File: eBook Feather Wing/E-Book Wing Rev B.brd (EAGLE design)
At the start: 77.5 x 107.4 mm, 92 parts, among them IC1 MCP23008/SO, IC2 23K256-I/SN, J1 MJ-3502N, Q1 IRLML0100, Q2 BSS138, Q3 DMG3415, SW1 SPDT_SWITCH

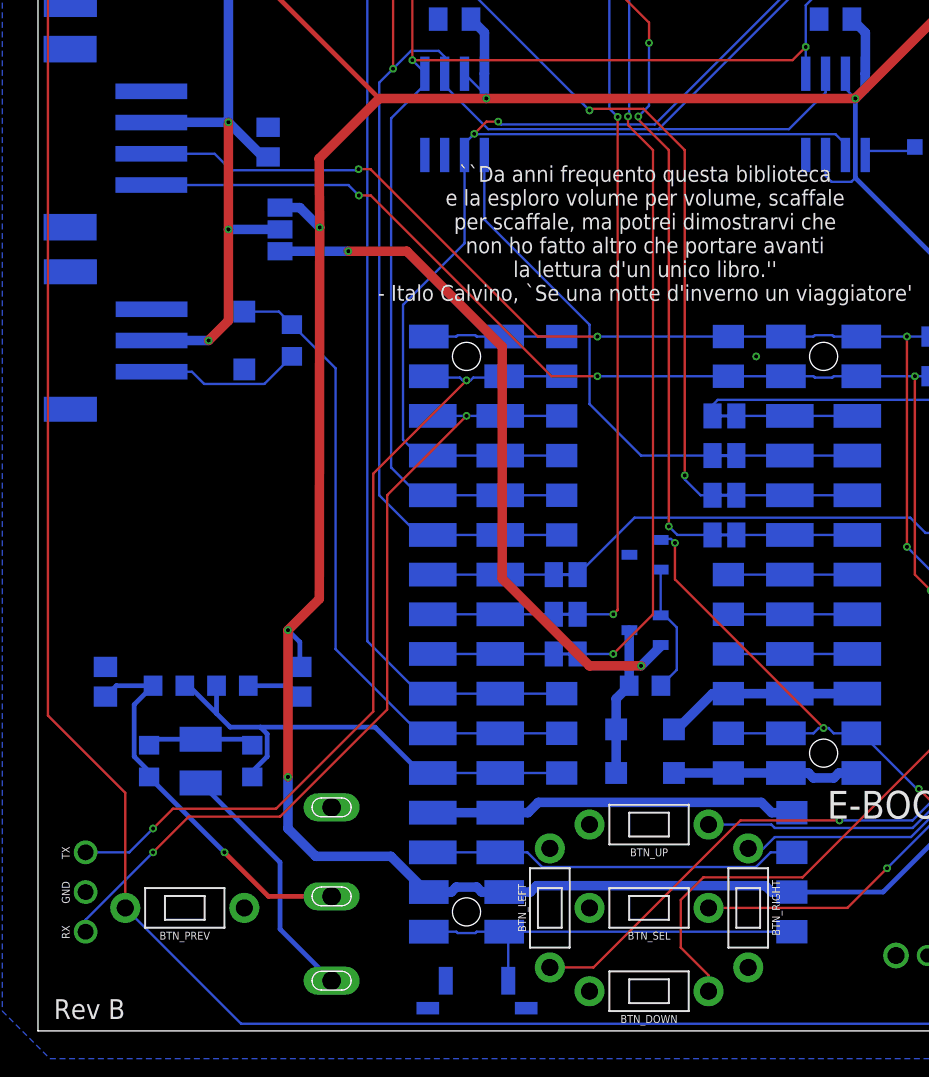
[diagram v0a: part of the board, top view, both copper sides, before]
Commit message: remove 5V option, more complicated than I thought
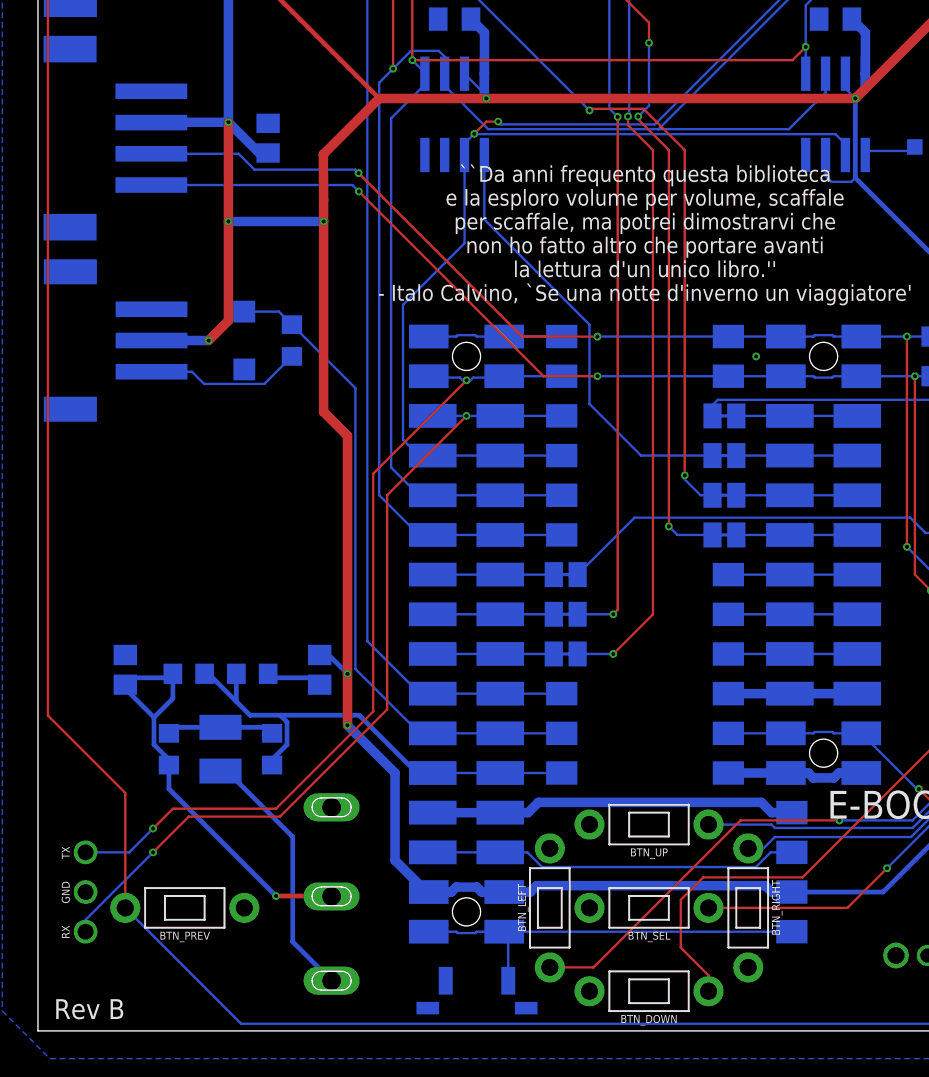
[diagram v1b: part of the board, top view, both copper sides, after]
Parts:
- removed D6, D7: MBR120, microbuilder:SOD-123
- removed Q2: BSS138, pygamer-microbuilder:SOT23-R
- removed Q3: DMG3415, pygamer-microbuilder:SOT23-R
- removed R10: 100K, microbuilder:_0805MP
- removed SJ1: (no value), pygamer-microbuilder:SOLDERJUMPER_2WAY_OPEN_NOPASTE
- moved R9 1.48 mm to (8.13, 18.0)
- moved C6 1.48 mm to (11.4, 18.0)
- moved FB1 1.48 mm to (17.8, 23.1)
- moved FB2 1.48 mm to (5.33, 23.1)
- moved R6 1.48 mm to (13.5, 22.9)
- moved R7 1.48 mm to (9.40, 22.9)
- moved R8 1.48 mm to (14.7, 18.0)
- moved C1 0.25 mm to (14.5, 57.1)
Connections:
- removed net !EN: Q2.1, Q3.2, R10.1
- removed net +5V: Q2.2, SJ1.1
- removed net N$7: D6.C, D7.C, Q2.3, R10.2
- removed net V+: A1_PORT.2, A2_PORT.2, C1.1, I2C.2, SJ1.2
- net +3V3: now also A1_PORT.2, A2_PORT.2, C1.1, I2C.2; no longer SJ1.3
- net EN: no longer Q3.1
- net GND: no longer Q3.3
- net VBAT: no longer D7.A
- net VBUS: no longer D6.A
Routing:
- net V+: track 45.5 -> 0.00 mm, vias 3 -> 0
- net +5V: track 44.7 -> 0.00 mm, vias 2 -> 0
- net +3V3: track 298.3 -> 338.3 mm, vias 9 -> 12
- net EN: track 42.5 -> 25.5 mm, vias 3 -> 1
- net N$7: track 9.50 -> 0.00 mm
- net !EN: track 8.43 -> 0.00 mm
- net VBUS: track 12.7 -> 8.26 mm
- net VBAT: track 12.3 -> 8.77 mm
- net AGND: track 24.9 -> 27.7 mm
- net A0: track 32.0 -> 31.0 mm
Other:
- board text added: "ENABLE_SWITCH"
- board text added: "HEADPHONE JACK"
- board text added: "The DAC on A0 drives mono jack J1. Ferrite beads FB1 & FB2 isolate this analog circuit to reduce noise. R6 & R7 act as a voltage divider on 3V to set the bias of the output signal. Then C6, a large coupling capacitor, lets audible frequencies pass while blocking any DC bias."
- board text removed: "+VOLTAGE SELECT!"
- board text removed: "5V"
- board text removed: "5V to ports v"
- board text removed: "Easy way: Close SJ1 to 3V and you're done. If you want to power 5V devices, close SJ1 to 5V and populate: D6 & D7 (to get the higher of VBAT & VBUS), Q3 (to invert EN), Q2 (to switch 5V on when Feather is enabled) and R10 (pullup for !EN!)."
- board text removed: "HEADPHONE JACK (A0)"
- board text removed: "Only needed for 5V on <-JST ports! See voltage select note at right."
- board text removed: "higher power"

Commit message: final commit of rev B as submitted to OSH Park
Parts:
- added BTN_LOCK: SPST_TACTILE_SWITCHRA, My Stuff:TL3330AF130QG
- added FID1, FID2, FID3, FID4: FIDUCIAL_1MM, microbuilder:FIDUCIAL_1MM
- added JP2: (no value), adafruit:1X01
- added U$1, U$4, U$5, U$7: MOUNTINGHOLE2.5, microbuilder:MOUNTINGHOLE_2.5_PLATED
- moved JP1 100.2 mm to (8.64, 109.0), turned to 0 degrees
- moved FB1 4.89 mm to (15.5, 18.8)
- moved FB2 4.89 mm to (3.05, 18.8)
- moved C6 4.89 mm to (9.14, 13.7)
- moved R8 4.89 mm to (12.4, 13.7)
- moved R9 4.89 mm to (5.84, 13.7)
- moved R6 4.89 mm to (11.2, 18.5)
- moved R7 4.89 mm to (7.11, 18.5)
- moved GOLD_ORB_SM1 4.42 mm to (68.1, 4.06)
- moved MICROSD 0.38 mm to (61.1, 82.0)
- moved BTN_NEXT_ALT 0.15 mm to (74.3, 90.9)
- moved BTN_PREV_ALT 0.15 mm to (2.64, 91.4)
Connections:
- new net BTN_LOCK: BTN_LOCK.P$1, IC1.17
- net +3V3: now also JP2.1
- net GND: now also BTN_LOCK.P$2
- net SD_CD: no longer IC1.17
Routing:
- net BTN_LOCK: track 0.00 -> 91.0 mm, vias 0 -> 2
- net SD_CD: track 57.4 -> 0.00 mm, vias 2 -> 0
- net RX: track 54.8 -> 86.9 mm, vias 2 -> 3
- net +3V3: track 338.3 -> 367.2 mm, vias 12 -> 11
- net TX: track 54.5 -> 83.0 mm, vias 2 -> 3
- net GND: track 23.5 -> 0.00 mm, vias 5 -> 8
- net A0: track 31.0 -> 37.7 mm, vias 0 -> 2
- net AUDIO_OUT: track 16.6 -> 13.9 mm
- net AGND: track 27.7 -> 30.1 mm
- net BTN_LEFT: track 54.6 -> 55.4 mm
- net PREVGL: track 44.4 -> 43.8 mm
- net BTN_NEXT: track 88.7 -> 89.2 mm
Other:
- board size 77.5 x 107.4 mm -> 77.5 x 111.3 mm
- board text added: ">1 NC 2 N-Channel MOSFET Gate Drive Control 3 Current Sense Input for Control Loop 4 Negative Gate driving voltage 5 Positive Gate driving voltage 6 Clock for external LM75 temp sensor 7 Data for external LM75 temp sensor 8 Bus selection pin (tied to GND) 9 Busy state output pin (EBSY) 10 Reset (ERST) 11 Data / Command input pin (EDC) 12 Chip Select input pin (ECS) 13 Serial clock pin (SPI: SCK) 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"
- board text added: "A microSD card interfaces with the Feather mainboard via the SPI interface (MISO, MOSI, SCK, SDCS). C2 is a filtering cap for the SD card's power supply."
- board text added: "BTN_LOCK"
- board text added: "Bits: 0: LEFT 1: DOWN 2: UP 3: RIGHT 4: SEL 5: PREV 6: NEXT 7: LOCK"
- board text added: "Project info:"
- board text added: "The 23K256-I/SN SRAM chip provides a buffer for the display. It uses the SPI interface + SRCS. A B&W 400x300 display requires 15000 bytes; if you have that RAM to spare, omit this chip (and C4)."
- board text added: "The DAC on A0 drives mono headphone jack J1. FB1 & FB2 are ferrite beads that isolate this analog circuit from the rest of the board. R6 & R7 act as a voltage divider on the isolated 3V to set the bias of the output signal. C6 acts as a coupling capacitor; it lets the AC component of the output signal pass to the headphone jack, while blocking the DC component."
- board text added: "The MCP23008 provides eight additional GPIO pins via the I2C interface. It connects to all buttons except for RESET. R3 and R4 are the pull-up resistors for, respectively, SDA and SCL. This chip is required to use the buttons, unless you just want a few wired directly to GPIO pads. Capacitor C3 filters power."
- board text added: "These are the Feather's UART pins, plus a 3V pin if you need to power something like a GPS. Toss some right angle header on here, it might prove useful."
- board text added: "This bit is unrelated, just an extra spot for <- a `Next Page' button."
- board text added: "github.com/joeycastillo/The-Open-Book"
- board text removed: ">1 NC 2 N-Channel MOSFET Gate Drive Control 3 Current Sense Input for Control Loop 4 Negative Gate driving voltage 5 Positive Gate driving voltage 6 Clock for external LM75 temp sensor 7 Data for external LM75 temp sensor 8 Bus selection pin (tied to GND) 9 Busy state output pin 10 Reset 11 Data / Command control pin 12 Chip Select input pin 13 Serial clock pin (SPI) 14 Serial data pin (SPI) 15 P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"
- board text removed: "A microSD card interfaces with the Feather mainboard via the SPI interface (MISO, MOSI, SCK, SDCS). The card detect line is available via the GPIO expander's high bit. C2 is a filtering cap for the SD card's power supply."
- board text removed: "Bits: 0: LEFT 1: DOWN 2: UP 3: RIGHT 4: SEL 5: PREV 6: NEXT 7: SD CD"
- board text removed: "CARD DET"
- board text removed: "I brought the Feather's UART pins out here. Might as well toss some right angle header on JP1, might turn out to be useful."
- board text removed: "The 23K256-I/SN SRAM chip provides a buffer for the display. It uses the SPI interface + SRCS. A B&W 400x300 display requires 16000 bytes; if you have that RAM to spare, omit this chip (and C4)."
- board text removed: "The DAC on A0 drives mono jack J1. Ferrite beads FB1 & FB2 isolate this analog circuit to reduce noise. R6 & R7 act as a voltage divider on 3V to set the bias of the output signal. Then C6, a large coupling capacitor, lets audible frequencies pass while blocking any DC bias."
- board text removed: "The MCP23008 provides eight additional GPIO pins via the I2C interface. It connects to all buttons (except for RESET) as well as the SD slot's card detect signal. R3 and R4 are the pull-up resistors for SDA and SCL, respectively. This chip is required to use the buttons unless you just want a few wired directly to GPIO pads. Capacitor C3 filters power."
- board text removed: "This bit is unrelated, just <- an extra spot for a `Next Page' button."

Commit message: final tweaks and BOM for rev B
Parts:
- L1: value 68uH -> 10uH
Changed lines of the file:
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@@
 <attribute name="VALUE" x="44.45" y="78.486" size="0.508" layer="28" font="vector" ratio="18" rot="MR270" align="center"/>
 </element>
-<element name="L1" library="microbuilder" package="INDUCTOR_4X4MM_NR401" value="68uH" x="38.1" y="77.216" smashed="yes" rot="MR90">
+<element name="L1" library="microbuilder" package="INDUCTOR_4X4MM_NR401" value="10uH" x="38.1" y="77.216" smashed="yes" rot="MR90">
 <attribute name="NAME" x="38.1" y="74.676" size="0.508" layer="26" font="vector" ratio="18" rot="MR0" align="center"/>
 <attribute name="VALUE" x="41.3" y="75.216" size="0.508" layer="28" font="vector" ratio="18" rot="MR90" align="center"/>
